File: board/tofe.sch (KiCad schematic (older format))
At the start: 14 parts, among them P302 TOFE-8X, P303 DEBUG

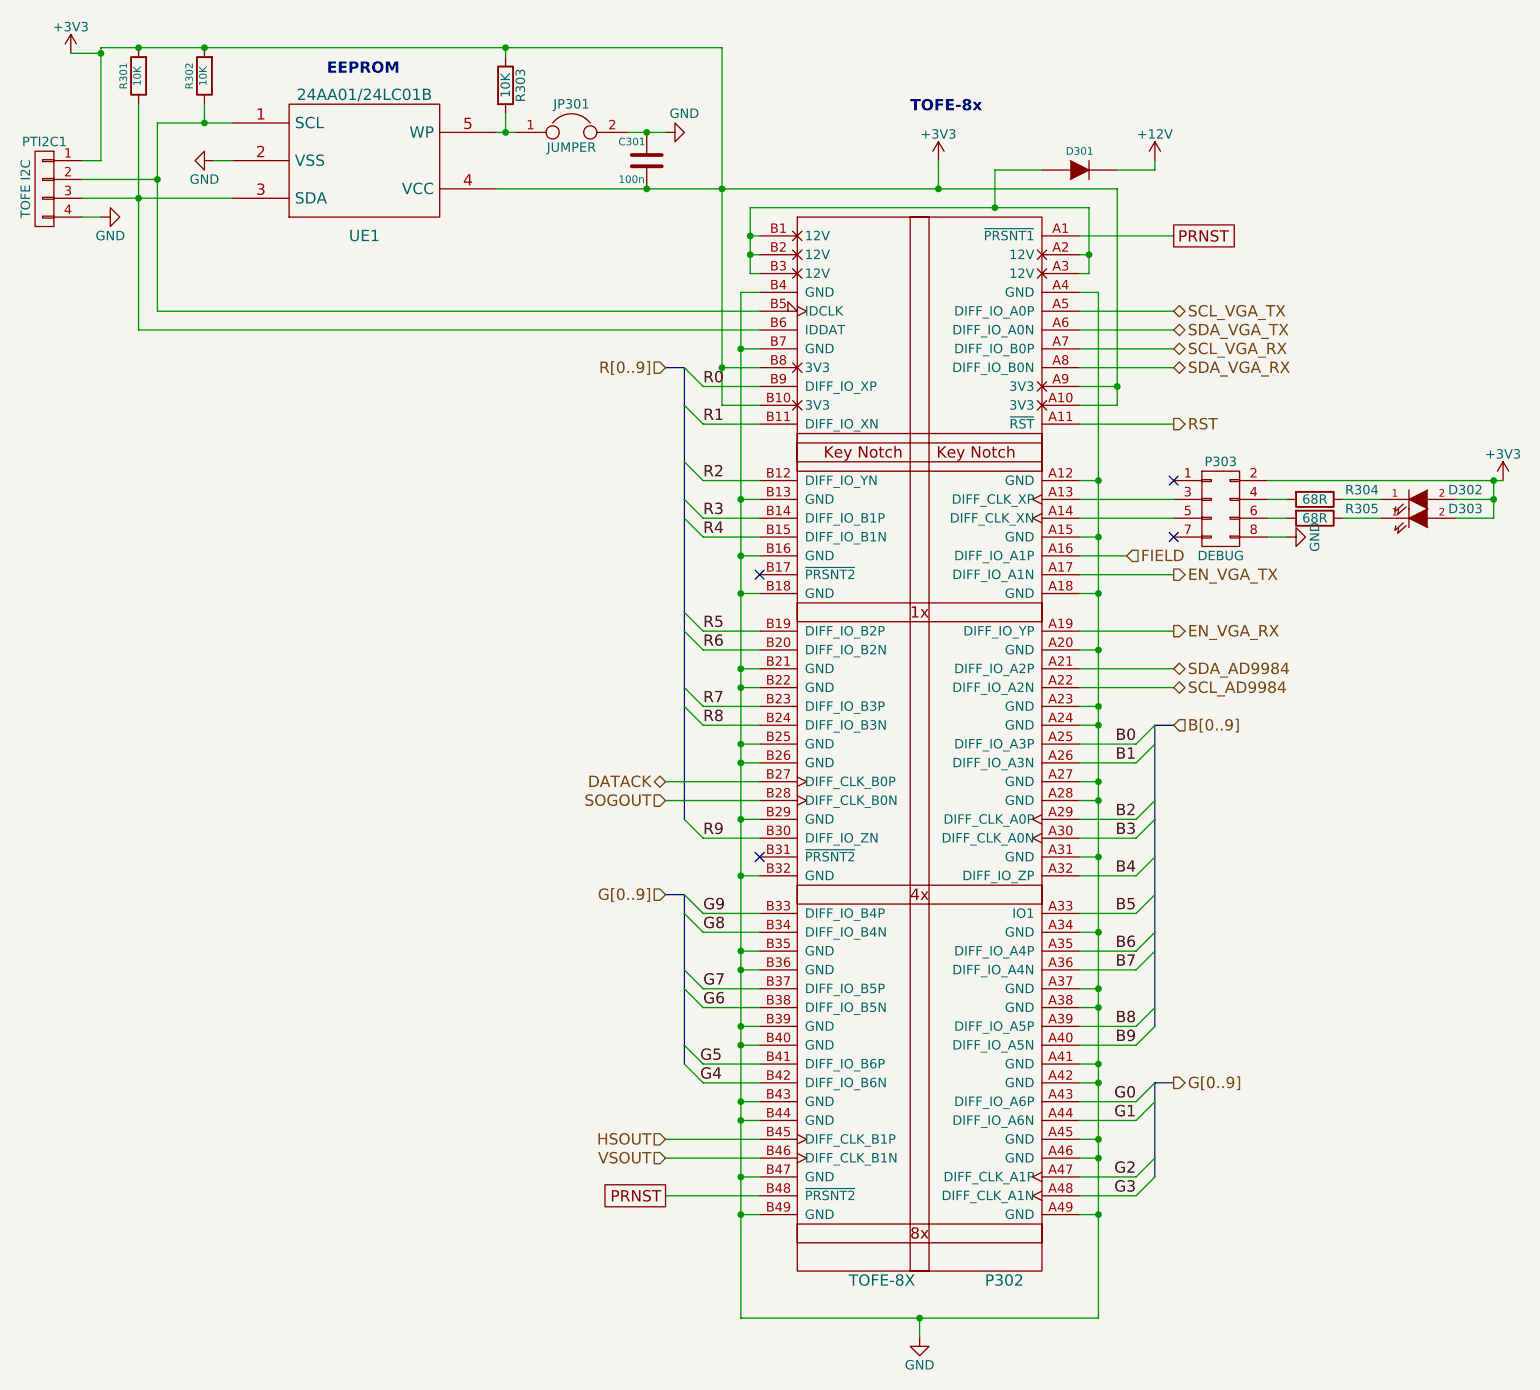
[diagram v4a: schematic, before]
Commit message: Updating net names.
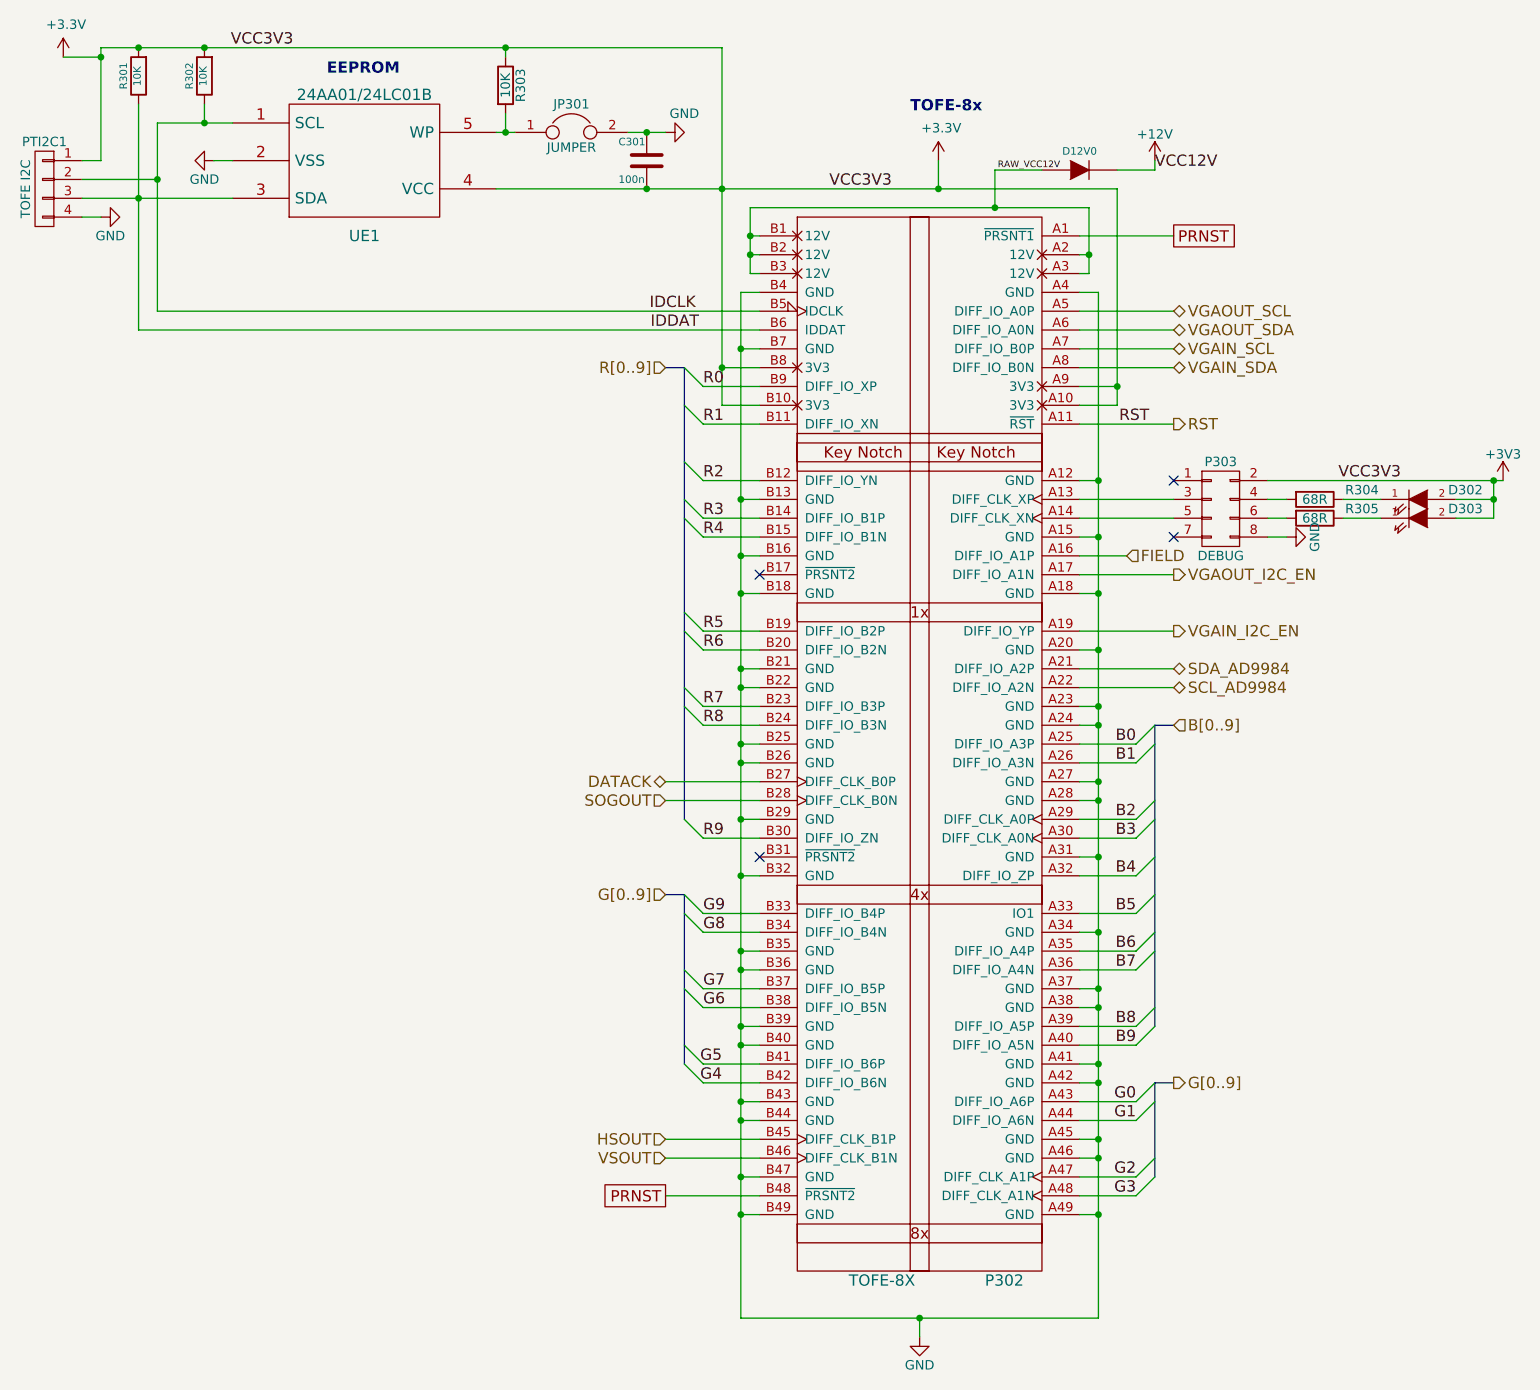
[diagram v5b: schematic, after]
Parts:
- renumbered D301 to D12V0
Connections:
- net RAW_VCC12V: now reaches D12V0.1 (A), P302.A2 (12V), P302.A3 (12V), P302.B1 (12V), P302.B2 (12V), P302.B3 (12V)
- net IDCLK: now reaches P302.B5 (IDCLK), PTI2C1.2 (P2), R302.1, UE1.1 (SCL)
- net IDDAT: now reaches P302.B6 (IDDAT), PTI2C1.3 (P3), R301.1, UE1.3 (SDA)
- net EN_VGA_RX renamed VGAIN_I2C_EN
- net EN_VGA_TX renamed VGAOUT_I2C_EN
- net SCL_VGA_RX renamed VGAIN_SCL
- net SCL_VGA_TX renamed VGAOUT_SCL
- net SDA_VGA_RX renamed VGAIN_SDA
- net SDA_VGA_TX renamed VGAOUT_SDA
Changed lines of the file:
@@
 TOFE-8x
 $Comp
-L DIODE D301
+L DIODE D12V0
 U 1 1 561CAC76
 P 6300 1300
-F 0 "D301" H 6300 1400 40  0000 C CNN
+F 0 "D12V0" H 6300 1400 40  0000 C CNN
 F 1 "DIODE" H 6300 1200 40  0001 C CNN
 F 2 "Diodes_SMD:SMB_Handsoldering" H 6300 1300 60  0001 C CNN
@@
 B[0..9]
 Text HLabel 6800 2050 2    60   BiDi ~ 0
-SCL_VGA_TX
+VGAOUT_SCL
 Text HLabel 6800 2150 2    60   BiDi ~ 0
-SDA_VGA_TX
+VGAOUT_SDA
 Text HLabel 6800 2250 2    60   BiDi ~ 0
-SCL_VGA_RX
+VGAIN_SCL
 Text HLabel 6800 2350 2    60   BiDi ~ 0
-SDA_VGA_RX
-$Comp
-L GND #PWR015
+VGAIN_SDA
+$Comp
+L GND #PWR19
 U 1 1 5641057B
 P 5450 7500
-F 0 "#PWR015" H 5450 7250 50  0001 C CNN
+F 0 "#PWR19" H 5450 7250 50  0001 C CNN
 F 1 "GND" H 5450 7350 50  0000 C CNN
 F 2 "" H 5450 7500 60  0000 C CNN
@@
 $EndComp
 $Comp
-L GND #PWR016
+L GND #PWR18
 U 1 1 56410719
 P 4100 1100
-F 0 "#PWR016" H 4100 850 50  0001 C CNN
+F 0 "#PWR18" H 4100 850 50  0001 C CNN
 F 1 "GND" V 4200 1000 50  0000 C CNN
 F 2 "" H 4100 1100 60  0000 C CNN
@@
 $EndComp
 $Comp
-L GND #PWR017
+L GND #PWR17
 U 1 1 564109C3
 P 1700 1250
-F 0 "#PWR017" H 1700 1000 50  0001 C CNN
+F 0 "#PWR17" H 1700 1000 50  0001 C CNN
 F 1 "GND" V 1800 1200 50  0000 C CNN
 F 2 "" H 1700 1250 60  0000 C CNN
@@
 $EndComp
 $Comp
-L +3V3 #PWR018
-U 1 1 56412B64
-P 5550 1250
-F 0 "#PWR018" H 5550 1100 50  0001 C CNN
-F 1 "+3V3" H 5550 1390 50  0000 C CNN
-F 2 "" H 5550 1250 60  0000 C CNN
-F 3 "" H 5550 1250 60  0000 C CNN
-	1    5550 1250
-	1    0    0    -1
-$EndComp
-$Comp
-L +12V #PWR019
+L +12V #PWR21
 U 1 1 56412B95
 P 6700 1250
-F 0 "#PWR019" H 6700 1100 50  0001 C CNN
+F 0 "#PWR21" H 6700 1100 50  0001 C CNN
 F 1 "+12V" H 6700 1390 50  0000 C CNN
 F 2 "" H 6700 1250 60  0000 C CNN
@@
 Connection ~ 4000 1100
 Wire Wire Line
-	1400 2050 1400 1050
+	1400 1050 1400 2050
 Connection ~ 1650 1050
 Wire Wire Line
@@
 	6700 6150 6700 6650
 Wire Bus Line
-	6700 5850 6700 4250
+	6700 4250 6700 5850
 Wire Wire Line
 	6300 3950 6800 3950
@@
 Connection ~ 8500 2950
 Wire Wire Line
-	8300 3150 8500 3150
+	8500 3150 8300 3150
 Connection ~ 8500 3050
 Wire Wire Line
@@
 Connection ~ 1400 1350
 $Comp
-L GND #PWR020
+L GND #PWR16
 U 1 1 56931407
 P 1100 1550
-F 0 "#PWR020" H 1100 1300 50  0001 C CNN
+F 0 "#PWR16" H 1100 1300 50  0001 C CNN
 F 1 "GND" V 1000 1500 50  0000 C CNN
 F 2 "" H 1100 1550 50  0000 C CNN
@@
 $EndComp
 Text HLabel 6800 3450 2    60   Output ~ 0
-EN_VGA_TX
+VGAOUT_I2C_EN
 Text HLabel 6800 3750 2    60   Output ~ 0
-EN_VGA_RX
+VGAIN_I2C_EN
 Wire Wire Line
 	6300 3450 6800 3450
@@
 	6300 3750 6800 3750
 $Comp
-L +3V3 #PWR021
+L +3V3 #PWR23
 U 1 1 579700B0
 P 8550 2950
-F 0 "#PWR021" H 8550 2800 50  0001 C CNN
+F 0 "#PWR23" H 8550 2800 50  0001 C CNN
 F 1 "+3V3" H 8550 3090 50  0000 C CNN
 F 2 "" H 8550 2950 60  0000 C CNN
@@
 RST
 Wire Wire Line
-	8500 3150 8500 2950
+	8500 2950 8500 3150
 Text HLabel 6550 3350 2    60   Input ~ 0
 FIELD
 $Comp
-L GND #PWR022
+L GND #PWR22
 U 1 1 579E0967
 P 7400 3250
-F 0 "#PWR022" H 7400 3000 50  0001 C CNN
+F 0 "#PWR22" H 7400 3000 50  0001 C CNN
 F 1 "GND" H 7400 3100 50  0000 C CNN
 F 2 "" H 7400 3250 50  0000 C CNN
@@
 NoConn ~ 6800 2950
 NoConn ~ 6800 3250
-$Comp
-L +3V3 #PWR023
-U 1 1 579E0C0C
-P 940 680
-F 0 "#PWR023" H 940 530 50  0001 C CNN
-F 1 "+3V3" H 940 820 50  0000 C CNN
-F 2 "" H 940 680 60  0000 C CNN
-F 3 "" H 940 680 60  0000 C CNN
-	1    940  680
-	1    0    0    -1
-$EndComp
-Wire Wire Line
-	940  680  1100 680
-Connection ~ 1100 680
+Wire Wire Line
+	900  700  1100 700
+Connection ~ 1100 700
+$Comp
+L +3.3V #PWR20
+U 1 1 57A326A4
+P 5550 1250
+F 0 "#PWR20" H 5550 1100 50  0001 C CNN
+F 1 "+3.3V" H 5565 1423 50  0000 C CNN
+F 2 "" H 5550 1250 50  0000 C CNN
+F 3 "" H 5550 1250 50  0000 C CNN
+	1    5550 1250
+	1    0    0    -1
+$EndComp
+$Comp
+L +3.3V #PWR15
+U 1 1 57A328B1
+P 900 700
+F 0 "#PWR15" H 900 550 50  0001 C CNN
+F 1 "+3.3V" H 915 873 50  0000 C CNN
+F 2 "" H 900 700 50  0000 C CNN
+F 3 "" H 900 700 50  0000 C CNN
+	1    900  700
+	1    0    0    -1
+$EndComp
+Text Label 4970 1400 0    60   ~ 0
+VCC3V3
+Text Label 6700 1300 0    60   ~ 0
+VCC12V
+Text Label 7675 2950 0    60   ~ 0
+VCC3V3
+Text Label 1790 650  0    60   ~ 0
+VCC3V3
+Text Label 4015 2050 0    60   ~ 0
+IDCLK
+Text Label 4020 2150 0    60   ~ 0
+IDDAT
+Text Label 6510 2650 0    60   ~ 0
+RST
+Text Label 5865 1300 0    35   ~ 0
+RAW_VCC12V
 $EndSCHEMATC

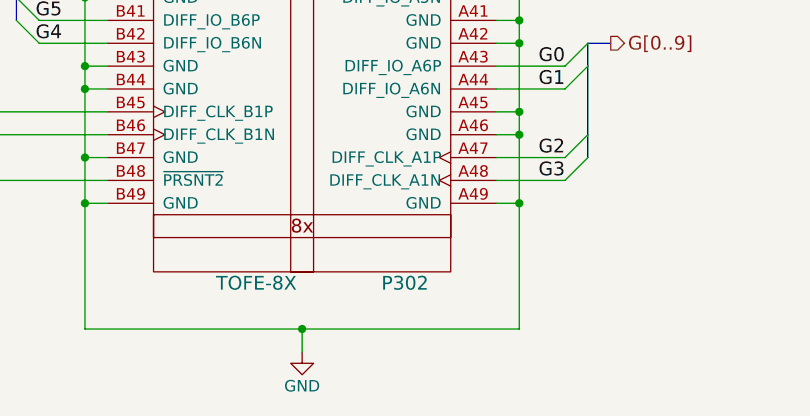
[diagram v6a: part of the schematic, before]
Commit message: ERC and removing 0 from vsync/hsync.
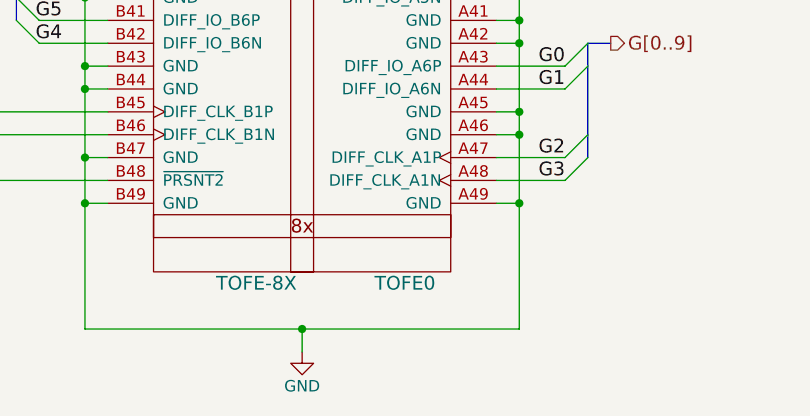
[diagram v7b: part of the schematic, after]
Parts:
- renumbered P302 to TOFE0
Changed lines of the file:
@@
 $EndDescr
 $Comp
-L TOFE-8X P302
+L TOFE-8X TOFE0
 U 1 1 561CABB0
 P 5900 4350
-F 0 "P302" H 5900 1500 60  0000 C CNN
+F 0 "TOFE0" H 5900 1500 60  0000 C CNN
 F 1 "TOFE-8X" H 5250 1500 60  0000 C CNN
 F 2 "TOFE_8X_HalfHeight:TOFE_8X_HalfHeight" H 4600 4050 60  0001 C CNN

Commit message: Giving things better names.
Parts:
- renumbered D302 to DDG1, D303 to DDG2, P303 to PDG0, R304 to RDG1, R305 to RDG2
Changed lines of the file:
@@
 	6300 3350 6550 3350
 $Comp
-L LED D302
+L LED DDG1
 U 1 1 56925C52
 P 8100 3050
-F 0 "D302" H 8350 3100 50  0000 C CNN
+F 0 "DDG1" H 8350 3100 50  0000 C CNN
 F 1 "LED" H 8100 2950 50  0001 C CNN
 F 2 "LEDs:LED_0805" H 8100 3050 50  0001 C CNN
@@
 $EndComp
 $Comp
-L R R304
+L R RDG1
 U 1 1 56925CE8
 P 7550 3050
-F 0 "R304" V 7500 3300 50  0000 C CNN
+F 0 "RDG1" V 7500 3300 50  0000 C CNN
 F 1 "68R" V 7550 3050 50  0000 C CNN
 F 2 "Resistors_SMD:R_0805_HandSoldering" V 7480 3050 50  0001 C CNN
@@
 	7700 3050 7900 3050
 $Comp
-L LED D303
+L LED DDG2
 U 1 1 56925FC5
 P 8100 3150
-F 0 "D303" H 8350 3200 50  0000 C CNN
+F 0 "DDG2" H 8350 3200 50  0000 C CNN
 F 1 "LED" H 8100 3050 50  0001 C CNN
 F 2 "LEDs:LED_0805" H 8100 3150 50  0001 C CNN
@@
 $EndComp
 $Comp
-L R R305
+L R RDG2
 U 1 1 56925FCB
 P 7550 3150
-F 0 "R305" V 7500 3400 50  0000 C CNN
+F 0 "RDG2" V 7500 3400 50  0000 C CNN
 F 1 "68R" V 7550 3150 50  0000 C CNN
 F 2 "Resistors_SMD:R_0805_HandSoldering" V 7480 3150 50  0001 C CNN
@@
 Connection ~ 3250 1100
 $Comp
-L CONN_02X04 P303
+L CONN_02X04 PDG0
 U 1 1 569346A3
 P 7050 3100
-F 0 "P303" H 7050 3350 50  0000 C CNN
+F 0 "PDG0" H 7050 3350 50  0000 C CNN
 F 1 "DEBUG" H 7050 2850 50  0000 C CNN
 F 2 "CON-SMD-2.54:TE-AMPMODU-MOD-II-4X2" H 7050 1900 50  0001 C CNN
